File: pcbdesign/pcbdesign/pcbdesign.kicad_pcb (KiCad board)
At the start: 2 copper layers, 50 x 50 mm, 29 parts, among them J1 Conn_01x06_Male, J2 USB_B_Mini, J3 Conn_Coaxial, SW1 SW_Push, U1 CMWX1ZZABZ-078, U2 LM1117ADJ

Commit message: Finish copper routing
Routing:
- net +3V3: track 0.00 -> 147.7 mm, vias 0 -> 5
- net /NRST: track 0.00 -> 56.2 mm, vias 0 -> 2
- net /D1: track 0.00 -> 39.9 mm, vias 0 -> 2
- net /D0: track 0.00 -> 38.7 mm, vias 0 -> 2
- net GND: track 0.00 -> 34.3 mm, vias 0 -> 1
- net /CS: track 0.00 -> 33.9 mm, vias 0 -> 2
- net +5V: track 0.00 -> 32.6 mm
- net Net-(R6-Pad1): track 0.00 -> 26.9 mm
- net /DC: track 0.00 -> 16.9 mm
- net /RES: track 0.00 -> 16.6 mm
- net Net-(C19-Pad1): track 0.00 -> 11.4 mm
- net /DAT: track 0.00 -> 9.68 mm
- net /SWDIO: track 0.00 -> 8.13 mm
- net Net-(BZ1-Pad1): track 0.00 -> 8.04 mm
- net /SWCLK: track 0.00 -> 7.44 mm
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- added copper zone on B.Cu, net GND
- added copper zone on F.Cu, net GND
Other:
- net class Power added: clearance 0.2, trace_width 1, via_dia 0.8, via_drill 0.4

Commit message: Finish review of board. Add text and logo to PCB
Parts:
- added C2: 0.1u, Capacitor_SMD:C_0805_2012Metric, F.Cu at (145.0, 108.5)
- added G***: LOGO, ProjectPCB:BEER_SMALL, B.Cu at (151.6, 100.3)
- added SW2: SW_Push, Button_Switch_SMD:SW_Push_1P1T_NO_6x6mm_H9.5mm, F.Cu at (145.0, 101.1)
- J2: value USB_B_Mini -> USB_B_Micro; footprint Connector_USB:USB_Mini-B_Wuerth_65100516121_Horizontal -> Connector_USB:USB_Micro-B_Wuerth_629105150521
- moved L1 4.96 mm to (176.2, 103.7), turned to 270 degrees
- moved C19 3.47 mm to (176.2, 100.0)
- moved J2 0.61 mm to (166.7, 124.6)
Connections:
- U1 pad 22: Net-(U1-Pad22) -> /BUTTON
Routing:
- net /BUTTON: track 0.00 -> 44.0 mm
- net Net-(C19-Pad1): track 11.4 -> 7.59 mm
- net Net-(C20-Pad1): track 7.08 -> 9.58 mm
- net GND: track 34.3 -> 36.3 mm, vias 1 -> 4
- net Net-(U1-Pad22): track 1.80 -> 0.00 mm
- net +5V: track 32.6 -> 33.7 mm
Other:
- board text added: "Because it's 3am somewhere!"
- board text added: "Made by:"
- board text added: "Mark Kyle Viktor"

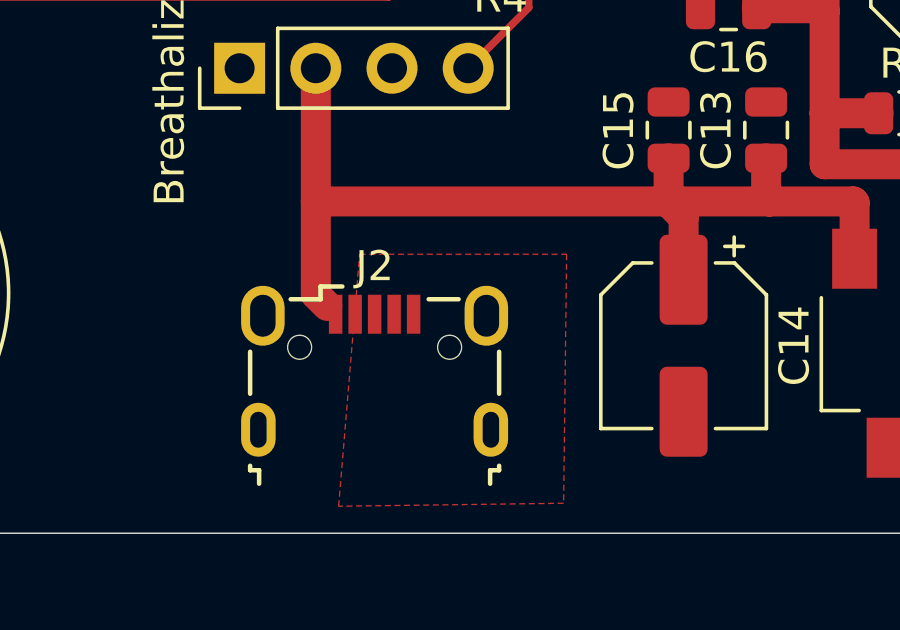
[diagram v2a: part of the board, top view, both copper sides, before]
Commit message: Add configs for running the debugging tools.
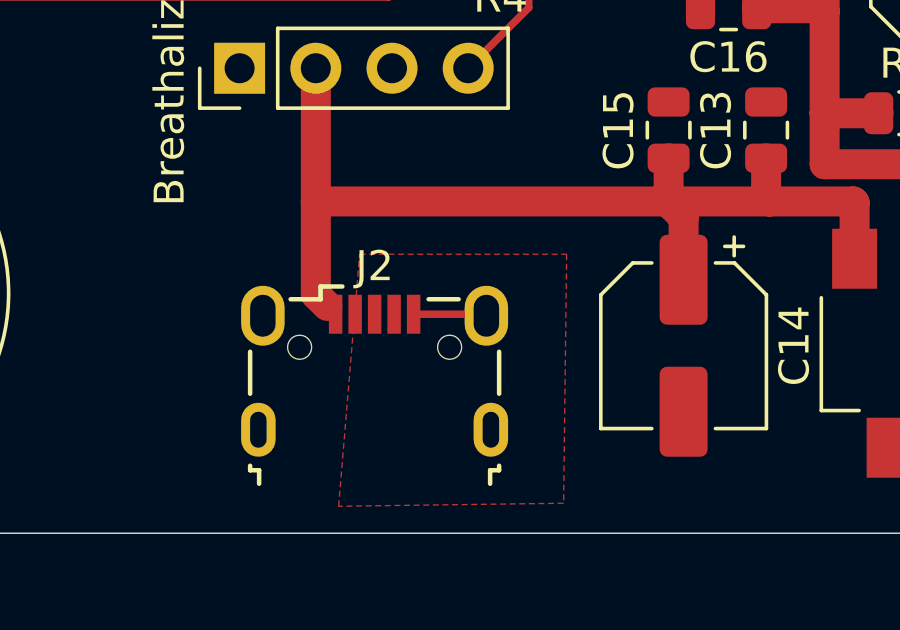
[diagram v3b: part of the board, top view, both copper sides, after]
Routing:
- net GND: track 36.3 -> 38.8 mm
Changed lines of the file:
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@@
     (thickness 1.6)
     (drawings 7)
-    (tracks 220)
+    (tracks 222)
     (zones 0)
     (modules 32)
@@
     (0 F.Cu signal)
     (31 B.Cu signal)
-    (32 B.Adhes user)
-    (33 F.Adhes user)
-    (34 B.Paste user)
-    (35 F.Paste user)
+    (32 B.Adhes user hide)
+    (33 F.Adhes user hide)
+    (34 B.Paste user hide)
+    (35 F.Paste user hide)
     (36 B.SilkS user)
-    (37 F.SilkS user)
+    (37 F.SilkS user hide)
     (38 B.Mask user)
     (39 F.Mask user)
-    (40 Dwgs.User user)
-    (41 Cmts.User user)
-    (42 Eco1.User user)
-    (43 Eco2.User user)
+    (40 Dwgs.User user hide)
+    (41 Cmts.User user hide)
+    (42 Eco1.User user hide)
+    (43 Eco2.User user hide)
     (44 Edge.Cuts user)
-    (45 Margin user)
-    (46 B.CrtYd user)
-    (47 F.CrtYd user)
-    (48 B.Fab user)
-    (49 F.Fab user)
+    (45 Margin user hide)
+    (46 B.CrtYd user hide)
+    (47 F.CrtYd user hide)
+    (48 B.Fab user hide)
+    (49 F.Fab user hide)
   )
   (setup
@@
     (solder_mask_min_width 0.25)
     (aux_axis_origin 0 0)
-    (visible_elements FFFFF77F)
+    (visible_elements FFFFFF7F)
     (pcbplotparams
-      (layerselection 0x010fc_ffffffff)
+      (layerselection 0x010d0_ffffffff)
       (usegerberextensions false)
       (usegerberattributes false)
@@
       (outputformat 1)
       (mirror false)
-      (drillshape 1)
+      (drillshape 0)
       (scaleselection 1)
-      (outputdirectory ""))
+      (outputdirectory "gerber/"))
   )
   (net 0 "")
@@
   (via (at 187.7 100.6) (size 0.8) (drill 0.4) (layers F.Cu B.Cu) (net 1))
   (segment (start 164.25 92.4) (end 164.25 93.35) (width 0.25) (layer F.Cu) (net 1))
+  (segment (start 170.375 122.7) (end 170.425 122.75) (width 0.25) (layer F.Cu) (net 1))
+  (segment (start 168 122.7) (end 170.375 122.7) (width 0.25) (layer F.Cu) (net 1))
   (segment (start 164.74 118.94) (end 176.46 118.94) (width 1) (layer F.Cu) (net 2))
   (segment (start 164.74 114.5) (end 164.74 118.94) (width 1) (layer F.Cu) (net 2))

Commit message: Update pcbdesign
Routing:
- net GND: track 38.8 -> 36.3 mm
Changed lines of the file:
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@@
-(kicad_pcb (version 20171130) (host pcbnew 5.1.5-1.fc31)
+(kicad_pcb (version 20171130) (host pcbnew "(5.1.5-0-10_14)")
   (general
     (thickness 1.6)
     (drawings 7)
-    (tracks 222)
+    (tracks 220)
     (zones 0)
     (modules 32)
@@
     (34 B.Paste user hide)
     (35 F.Paste user hide)
-    (36 B.SilkS user)
-    (37 F.SilkS user hide)
+    (36 B.SilkS user hide)
+    (37 F.SilkS user)
     (38 B.Mask user)
     (39 F.Mask user)
@@
     (solder_mask_min_width 0.25)
     (aux_axis_origin 0 0)
-    (visible_elements FFFFFF7F)
+    (visible_elements FFFFF77F)
     (pcbplotparams
       (layerselection 0x010d0_ffffffff)
@@
   (via (at 187.7 100.6) (size 0.8) (drill 0.4) (layers F.Cu B.Cu) (net 1))
   (segment (start 164.25 92.4) (end 164.25 93.35) (width 0.25) (layer F.Cu) (net 1))
-  (segment (start 170.375 122.7) (end 170.425 122.75) (width 0.25) (layer F.Cu) (net 1))
-  (segment (start 168 122.7) (end 170.375 122.7) (width 0.25) (layer F.Cu) (net 1))
   (segment (start 164.74 118.94) (end 176.46 118.94) (width 1) (layer F.Cu) (net 2))
   (segment (start 164.74 114.5) (end 164.74 118.94) (width 1) (layer F.Cu) (net 2))
